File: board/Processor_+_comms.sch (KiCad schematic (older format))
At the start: 50 parts, among them J1 53261-0471, U11 ATXMEGA256A3U-MH, U12 NTS0104, U13 CYPD3177, U14 TC1015-3.3VCT713

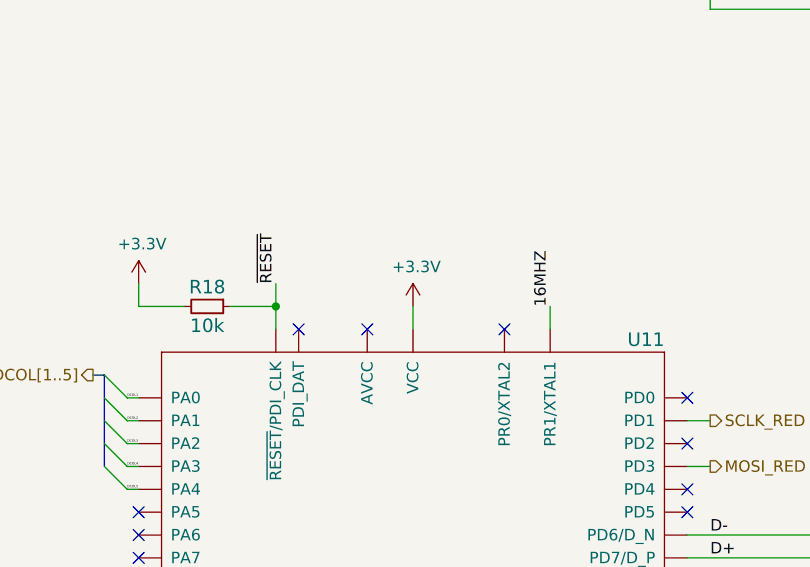
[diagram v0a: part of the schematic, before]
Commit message: Fixed AVCC on the processor being left floating which means PORTA/PORTB's GPIO and IO pads not being powered (this is undocumented!)
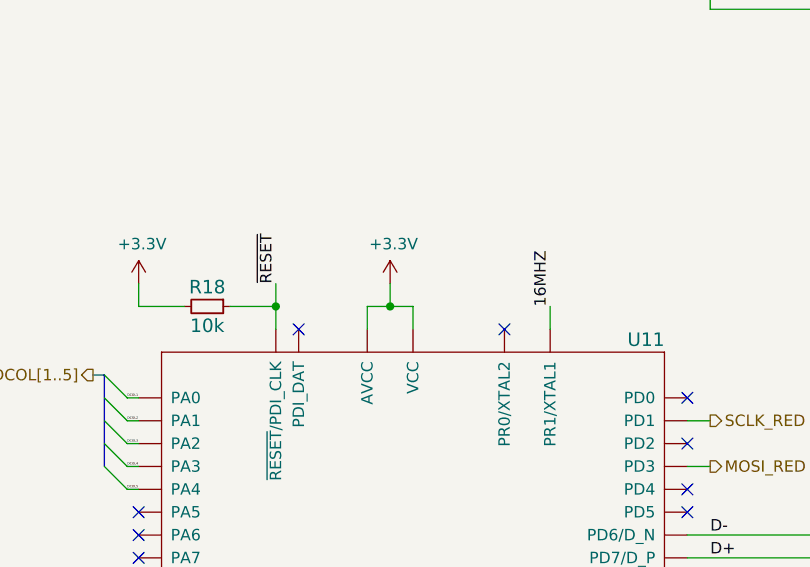
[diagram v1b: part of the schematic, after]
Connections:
- net +3V3: now also U11.61 (AVCC)
- no-connect marks 36 -> 35
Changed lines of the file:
@@
 L power:+3.3V #PWR039
 U 1 1 6F58A2B7
-P 5700 4100
-F 0 "#PWR039" H 5700 3950 50  0001 C CNN
-F 1 "+3.3V" H 5715 4273 50  0000 C CNN
-F 2 "" H 5700 4100 50  0001 C CNN
-F 3 "" H 5700 4100 50  0001 C CNN
-	1    5700 4100
+P 5600 4000
+F 0 "#PWR039" H 5600 3850 50  0001 C CNN
+F 1 "+3.3V" H 5615 4173 50  0000 C CNN
+F 2 "" H 5600 4000 50  0001 C CNN
+F 3 "" H 5600 4000 50  0001 C CNN
+	1    5600 4000
 	1    0    0    -1
 $EndComp
@@
 NoConn ~ 6900 4500
 NoConn ~ 6100 4200
-NoConn ~ 5500 4200
 NoConn ~ 5200 4200
 NoConn ~ 3400 2300
@@
 Wire Wire Line
 	9100 4500 9000 4500
+Wire Wire Line
+	5600 4000 5600 4100
+Wire Wire Line
+	5600 4100 5700 4100
+Wire Wire Line
+	5600 4100 5500 4100
+Wire Wire Line
+	5500 4100 5500 4200
 Wire Bus Line
 	4350 4400 4350 4800
 Wire Bus Line
 	7050 6300 7050 6800
+Connection ~ 5600 4100
 $EndSCHEMATC
